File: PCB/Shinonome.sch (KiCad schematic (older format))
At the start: 41 parts, among them J1 MJ-4PP-9, SW1 SW_PUSH, SW10 SW_PUSH, SW11 SW_PUSH, SW12 SW_PUSH, SW13 SW_PUSH, SW14 SW_PUSH, SW15 SW_PUSH, SW16 SW_PUSH, SW17 SW_PUSH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

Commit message: first pass pcb complete
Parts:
- added U2: ProMicro, kbd:ProMicro_v2_Backside, symbol kbd:ProMicro
- SW1, SW10, SW11, SW12, SW13, SW14, SW15, SW16, SW17, SW18, SW19, SW2, SW3, SW4, SW5, SW6, SW7, SW8, SW9: footprint kbd:CherryMX_Hotswap -> helix:MX_ALPS_PG1350_noLed
- U1: footprint kbd:ProMicro_v2 -> kbd:ProMicro_v2_Backside
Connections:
- net GND: now also U2.23 (GND), U2.3 (GND), U2.4 (GND)
- net VCC: now also U2.21 (VCC)
- net col0: now also U2.13 (B6)
- net col1: now also U2.14 (B2)
- net col2: now also U2.15 (B3)
- net col3: now also U2.16 (B1)
- net col4: now also U2.17 (F7)
- net col5: now also U2.18 (F6)
- net data: now also U2.2 (RX)
- net reset: now also U2.22 (RST)
- net row0: now also U2.9 (D7)
- net row1: now also U2.10 (E6)
- net row2: now also U2.11 (B4)
- net row3: now also U2.12 (B5)
- no-connect marks 9 -> 17
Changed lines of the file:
@@
 EESchema Schematic File Version 4
+LIBS:Shinonome-cache
 EELAYER 26 0
 EELAYER END
@@
 F 0 "U1" H 9550 3087 60  0000 C CNN
 F 1 "ProMicro" H 9550 2981 60  0000 C CNN
-F 2 "kbd:ProMicro_v2" H 9650 1000 60  0001 C CNN
+F 2 "kbd:ProMicro_v2_Backside" H 9650 1000 60  0001 C CNN
 F 3 "" H 9650 1000 60  0000 C CNN
 	1    9550 2050
@@
 F 0 "SW1" H 1750 1955 50  0000 C CNN
 F 1 "SW_PUSH" H 1750 1864 50  0000 C CNN
-F 2 "kbd:CherryMX_Hotswap" H 1750 1700 50  0001 C CNN
+F 2 "helix:MX_ALPS_PG1350_noLed" H 1750 1700 50  0001 C CNN
 F 3 "" H 1750 1700 50  0000 C CNN
 	1    1750 1700
@@
 F 0 "SW4" H 2650 1955 50  0000 C CNN
 F 1 "SW_PUSH" H 2650 1864 50  0000 C CNN
-F 2 "kbd:CherryMX_Hotswap" H 2650 1700 50  0001 C CNN
+F 2 "helix:MX_ALPS_PG1350_noLed" H 2650 1700 50  0001 C CNN
 F 3 "" H 2650 1700 50  0000 C CNN
 	1    2650 1700
@@
 F 0 "SW7" H 3550 1955 50  0000 C CNN
 F 1 "SW_PUSH" H 3550 1864 50  0000 C CNN
-F 2 "kbd:CherryMX_Hotswap" H 3550 1700 50  0001 C CNN
+F 2 "helix:MX_ALPS_PG1350_noLed" H 3550 1700 50  0001 C CNN
 F 3 "" H 3550 1700 50  0000 C CNN
 	1    3550 1700
@@
 F 0 "SW10" H 4450 1955 50  0000 C CNN
 F 1 "SW_PUSH" H 4450 1864 50  0000 C CNN
-F 2 "kbd:CherryMX_Hotswap" H 4450 1700 50  0001 C CNN
+F 2 "helix:MX_ALPS_PG1350_noLed" H 4450 1700 50  0001 C CNN
 F 3 "" H 4450 1700 50  0000 C CNN
 	1    4450 1700
@@
 F 0 "SW14" H 5350 1955 50  0000 C CNN
 F 1 "SW_PUSH" H 5350 1864 50  0000 C CNN
-F 2 "kbd:CherryMX_Hotswap" H 5350 1700 50  0001 C CNN
+F 2 "helix:MX_ALPS_PG1350_noLed" H 5350 1700 50  0001 C CNN
 F 3 "" H 5350 1700 50  0000 C CNN
 	1    5350 1700
@@
 F 0 "SW2" H 1750 2605 50  0000 C CNN
 F 1 "SW_PUSH" H 1750 2514 50  0000 C CNN
-F 2 "kbd:CherryMX_Hotswap" H 1750 2350 50  0001 C CNN
+F 2 "helix:MX_ALPS_PG1350_noLed" H 1750 2350 50  0001 C CNN
 F 3 "" H 1750 2350 50  0000 C CNN
 	1    1750 2350
@@
 F 0 "SW5" H 2650 2605 50  0000 C CNN
 F 1 "SW_PUSH" H 2650 2514 50  0000 C CNN
-F 2 "kbd:CherryMX_Hotswap" H 2650 2350 50  0001 C CNN
+F 2 "helix:MX_ALPS_PG1350_noLed" H 2650 2350 50  0001 C CNN
 F 3 "" H 2650 2350 50  0000 C CNN
 	1    2650 2350
@@
 F 0 "SW8" H 3550 2605 50  0000 C CNN
 F 1 "SW_PUSH" H 3550 2514 50  0000 C CNN
-F 2 "kbd:CherryMX_Hotswap" H 3550 2350 50  0001 C CNN
+F 2 "helix:MX_ALPS_PG1350_noLed" H 3550 2350 50  0001 C CNN
 F 3 "" H 3550 2350 50  0000 C CNN
 	1    3550 2350
@@
 F 0 "SW11" H 4450 2605 50  0000 C CNN
 F 1 "SW_PUSH" H 4450 2514 50  0000 C CNN
-F 2 "kbd:CherryMX_Hotswap" H 4450 2350 50  0001 C CNN
+F 2 "helix:MX_ALPS_PG1350_noLed" H 4450 2350 50  0001 C CNN
 F 3 "" H 4450 2350 50  0000 C CNN
 	1    4450 2350
@@
 F 0 "SW15" H 5350 2605 50  0000 C CNN
 F 1 "SW_PUSH" H 5350 2514 50  0000 C CNN
-F 2 "kbd:CherryMX_Hotswap" H 5350 2350 50  0001 C CNN
+F 2 "helix:MX_ALPS_PG1350_noLed" H 5350 2350 50  0001 C CNN
 F 3 "" H 5350 2350 50  0000 C CNN
 	1    5350 2350
@@
 F 0 "SW3" H 1750 3255 50  0000 C CNN
 F 1 "SW_PUSH" H 1750 3164 50  0000 C CNN
-F 2 "kbd:CherryMX_Hotswap" H 1750 3000 50  0001 C CNN
+F 2 "helix:MX_ALPS_PG1350_noLed" H 1750 3000 50  0001 C CNN
 F 3 "" H 1750 3000 50  0000 C CNN
 	1    1750 3000
@@
 F 0 "SW6" H 2650 3255 50  0000 C CNN
 F 1 "SW_PUSH" H 2650 3164 50  0000 C CNN
-F 2 "kbd:CherryMX_Hotswap" H 2650 3000 50  0001 C CNN
+F 2 "helix:MX_ALPS_PG1350_noLed" H 2650 3000 50  0001 C CNN
 F 3 "" H 2650 3000 50  0000 C CNN
 	1    2650 3000
@@
 F 0 "SW9" H 3550 3255 50  0000 C CNN
 F 1 "SW_PUSH" H 3550 3164 50  0000 C CNN
-F 2 "kbd:CherryMX_Hotswap" H 3550 3000 50  0001 C CNN
+F 2 "helix:MX_ALPS_PG1350_noLed" H 3550 3000 50  0001 C CNN
 F 3 "" H 3550 3000 50  0000 C CNN
 	1    3550 3000
@@
 F 0 "SW12" H 4450 3255 50  0000 C CNN
 F 1 "SW_PUSH" H 4450 3164 50  0000 C CNN
-F 2 "kbd:CherryMX_Hotswap" H 4450 3000 50  0001 C CNN
+F 2 "helix:MX_ALPS_PG1350_noLed" H 4450 3000 50  0001 C CNN
 F 3 "" H 4450 3000 50  0000 C CNN
 	1    4450 3000
@@
 F 0 "SW16" H 5350 3255 50  0000 C CNN
 F 1 "SW_PUSH" H 5350 3164 50  0000 C CNN
-F 2 "kbd:CherryMX_Hotswap" H 5350 3000 50  0001 C CNN
+F 2 "helix:MX_ALPS_PG1350_noLed" H 5350 3000 50  0001 C CNN
 F 3 "" H 5350 3000 50  0000 C CNN
 	1    5350 3000
@@
 F 0 "SW13" H 4450 3905 50  0000 C CNN
 F 1 "SW_PUSH" H 4450 3814 50  0000 C CNN
-F 2 "kbd:CherryMX_Hotswap" H 4450 3650 50  0001 C CNN
+F 2 "helix:MX_ALPS_PG1350_noLed" H 4450 3650 50  0001 C CNN
 F 3 "" H 4450 3650 50  0000 C CNN
 	1    4450 3650
@@
 F 0 "SW17" H 5350 3905 50  0000 C CNN
 F 1 "SW_PUSH" H 5350 3814 50  0000 C CNN
-F 2 "kbd:CherryMX_Hotswap" H 5350 3650 50  0001 C CNN
+F 2 "helix:MX_ALPS_PG1350_noLed" H 5350 3650 50  0001 C CNN
 F 3 "" H 5350 3650 50  0000 C CNN
 	1    5350 3650
@@
 F 0 "SW18" H 6250 3255 50  0000 C CNN
 F 1 "SW_PUSH" H 6250 3164 50  0000 C CNN
-F 2 "kbd:CherryMX_Hotswap" H 6250 3000 50  0001 C CNN
+F 2 "helix:MX_ALPS_PG1350_noLed" H 6250 3000 50  0001 C CNN
 F 3 "" H 6250 3000 50  0000 C CNN
 	1    6250 3000
@@
 F 0 "SW19" H 6250 3905 50  0000 C CNN
 F 1 "SW_PUSH" H 6250 3814 50  0000 C CNN
-F 2 "kbd:CherryMX_Hotswap" H 6250 3650 50  0001 C CNN
+F 2 "helix:MX_ALPS_PG1350_noLed" H 6250 3650 50  0001 C CNN
 F 3 "" H 6250 3650 50  0000 C CNN
 	1    6250 3650
@@
 	1    0    0    -1
 $EndComp
+$Comp
+L kbd:ProMicro U2
+U 1 1 5C5884A0
+P 9550 3650
+F 0 "U2" H 9550 4687 60  0000 C CNN
+F 1 "ProMicro" H 9550 4581 60  0000 C CNN
+F 2 "kbd:ProMicro_v2_Backside" H 9650 2600 60  0001 C CNN
+F 3 "" H 9650 2600 60  0000 C CNN
+	1    9550 3650
+	1    0    0    -1
+$EndComp
+$Comp
+L power:GND #PWR08
+U 1 1 5C5884A7
+P 10575 3000
+F 0 "#PWR08" H 10575 2750 50  0001 C CNN
+F 1 "GND" V 10580 2872 50  0000 R CNN
+F 2 "" H 10575 3000 50  0001 C CNN
+F 3 "" H 10575 3000 50  0001 C CNN
+	1    10575 3000
+	0    -1   -1   0
+$EndComp
+$Comp
+L power:VCC #PWR09
+U 1 1 5C5884AD
+P 10575 3200
+F 0 "#PWR09" H 10575 3050 50  0001 C CNN
+F 1 "VCC" V 10592 3328 50  0000 L CNN
+F 2 "" H 10575 3200 50  0001 C CNN
+F 3 "" H 10575 3200 50  0001 C CNN
+	1    10575 3200
+	0    1    1    0
+$EndComp
+$Comp
+L power:GND #PWR07
+U 1 1 5C5884B3
+P 8550 3250
+F 0 "#PWR07" H 8550 3000 50  0001 C CNN
+F 1 "GND" H 8555 3077 50  0000 C CNN
+F 2 "" H 8550 3250 50  0001 C CNN
+F 3 "" H 8550 3250 50  0001 C CNN
+	1    8550 3250
+	1    0    0    -1
+$EndComp
+Wire Wire Line
+	8850 3100 8550 3100
+Wire Wire Line
+	10250 3000 10575 3000
+Wire Wire Line
+	10250 3200 10575 3200
+Text GLabel 8575 3000 0    50   Input ~ 0
+data
+Wire Wire Line
+	8575 3000 8850 3000
+Text GLabel 10250 3100 2    50   Input ~ 0
+reset
+Text GLabel 8850 3700 0    50   Input ~ 0
+row0
+Text GLabel 8850 3800 0    50   Input ~ 0
+row1
+Text GLabel 8850 3900 0    50   Input ~ 0
+row2
+Text GLabel 8850 4000 0    50   Input ~ 0
+row3
+Text GLabel 10250 4000 2    50   Input ~ 0
+col0
+Text GLabel 10250 3900 2    50   Input ~ 0
+col1
+Text GLabel 10250 3800 2    50   Input ~ 0
+col2
+Text GLabel 10250 3700 2    50   Input ~ 0
+col3
+Text GLabel 10250 3600 2    50   Input ~ 0
+col4
+Text GLabel 10250 3500 2    50   Input ~ 0
+col5
+NoConn ~ 10250 3400
+NoConn ~ 10250 3300
+NoConn ~ 10250 2900
+NoConn ~ 8850 2900
+NoConn ~ 8850 3600
+NoConn ~ 8850 3500
+NoConn ~ 8850 3400
+NoConn ~ 8850 3300
+Wire Wire Line
+	8550 3100 8550 3200
+Wire Wire Line
+	8850 3200 8550 3200
+Connection ~ 8550 3200
+Wire Wire Line
+	8550 3200 8550 3250
 $EndSCHEMATC

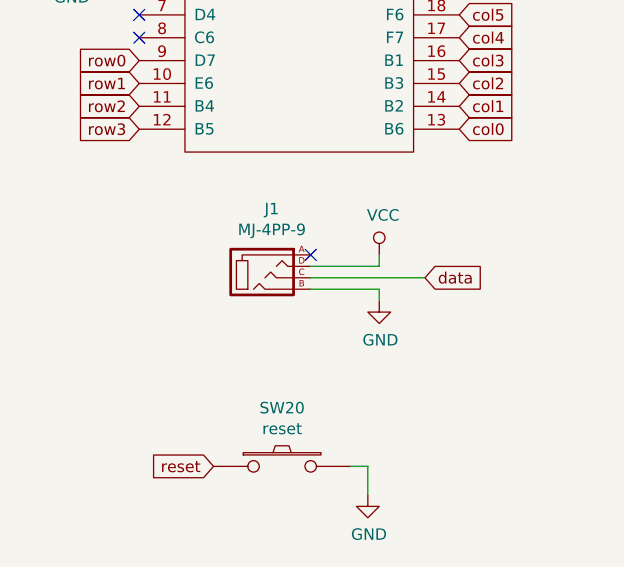
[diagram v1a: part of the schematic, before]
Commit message: fixed trrs jack incorrect pins
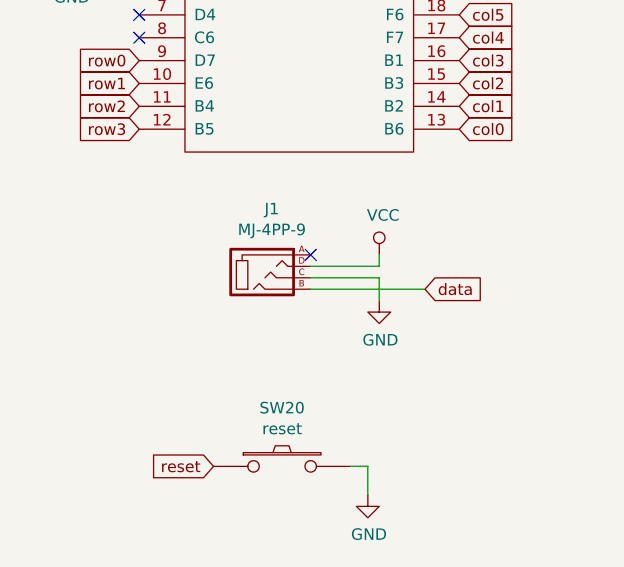
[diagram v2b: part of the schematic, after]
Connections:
- net GND: now also J1.C; no longer J1.B
- net data: now also J1.B; no longer J1.C
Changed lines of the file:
@@
 Wire Wire Line
 	9900 4600 9900 4550
-Wire Wire Line
-	9600 4700 9900 4700
-Wire Wire Line
-	9900 4700 9900 4750
-Text GLabel 10100 4650 2    50   Input ~ 0
+Text GLabel 10100 4700 2    50   Input ~ 0
 data
-Wire Wire Line
-	9600 4650 10100 4650
 Wire Wire Line
 	8850 1500 8550 1500
@@
 Wire Wire Line
 	8550 3200 8550 3250
+Wire Wire Line
+	9600 4650 9900 4650
+Wire Wire Line
+	9900 4650 9900 4750
+Wire Wire Line
+	9600 4700 10100 4700
 $EndSCHEMATC
